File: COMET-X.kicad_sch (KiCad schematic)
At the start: 17 parts, among them J1 ATX_12V_IN, U2 TPS5450ddar

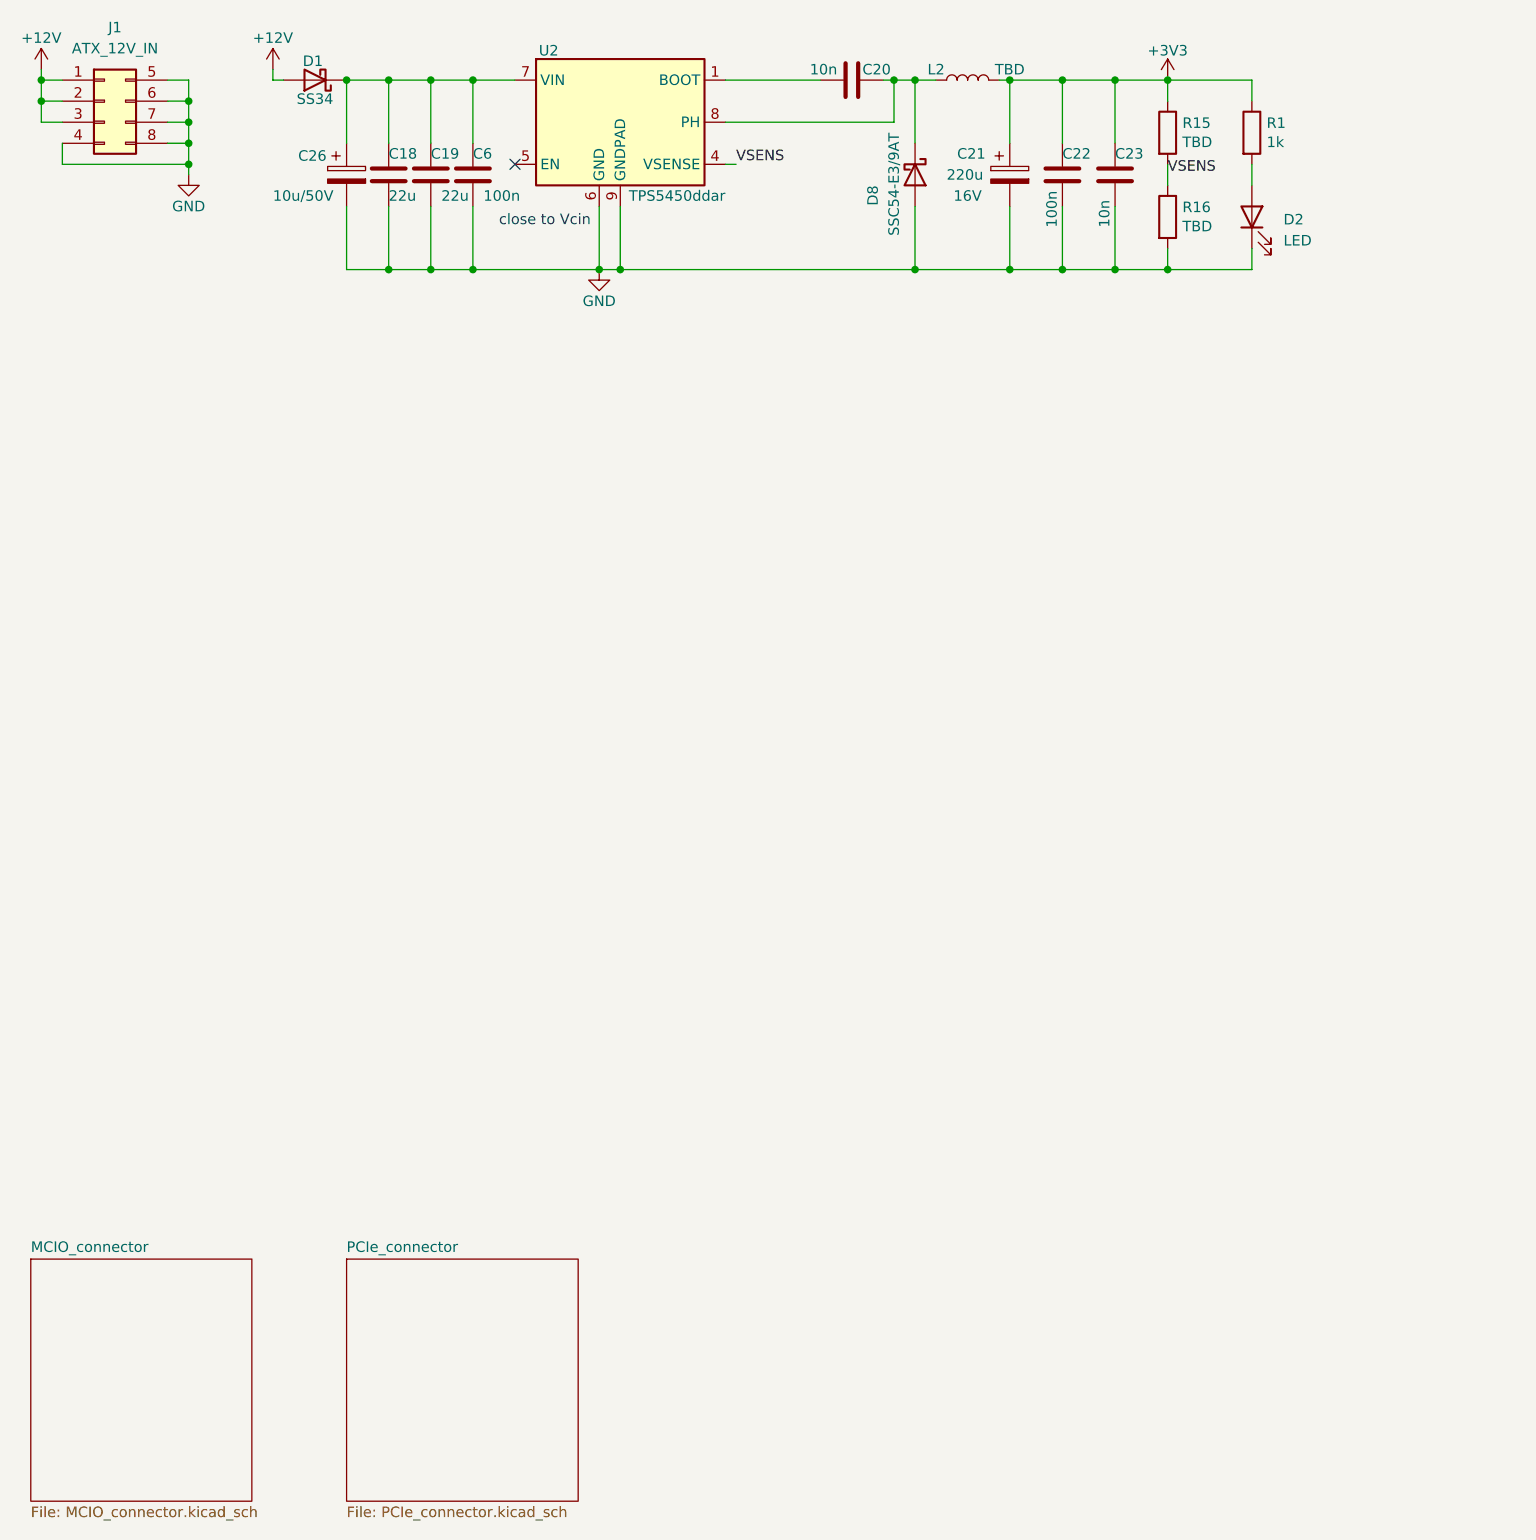
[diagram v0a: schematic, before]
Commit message: updated stackup and regulator
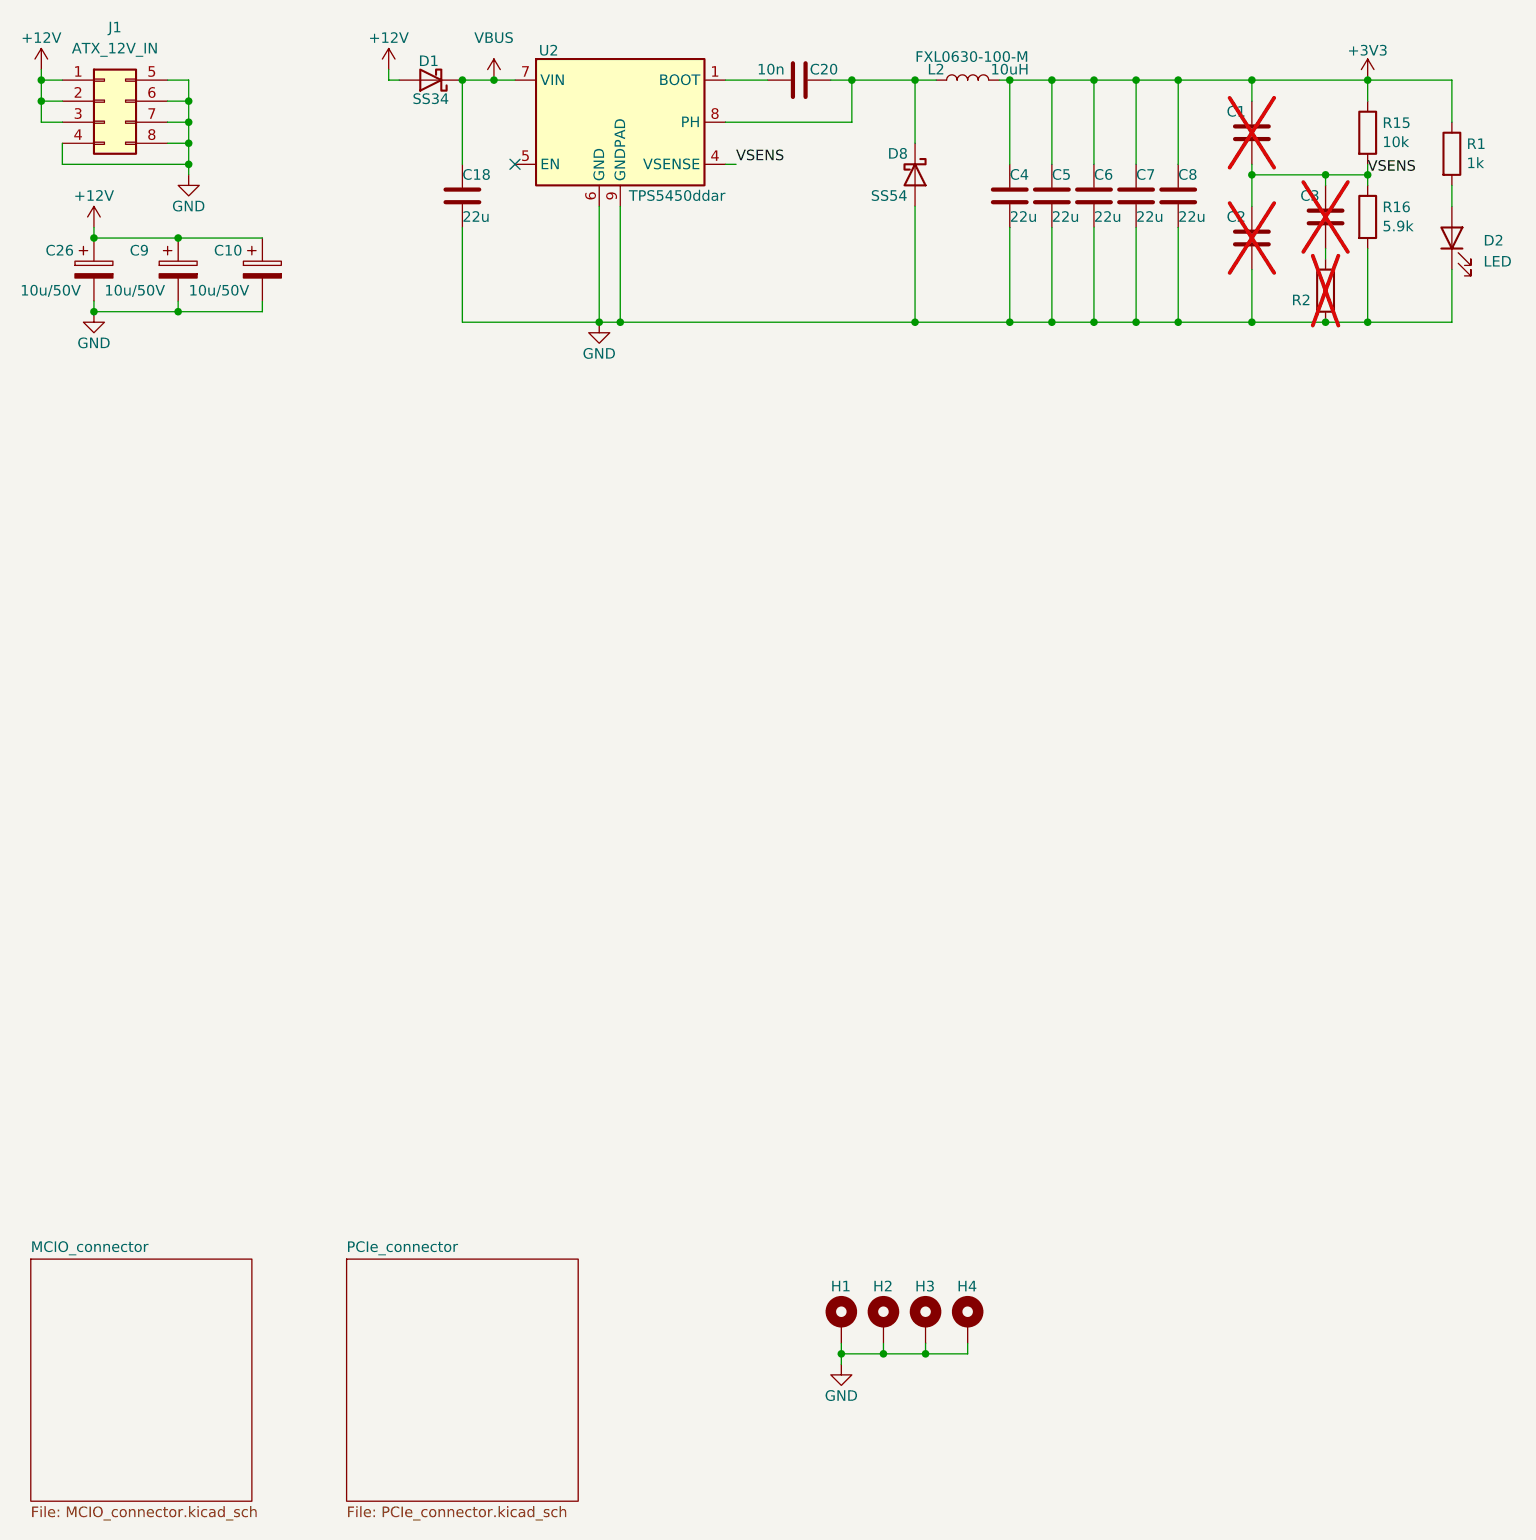
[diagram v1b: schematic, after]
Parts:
- removed C19: 22u, Capacitor_SMD:C_1206_3216Metric, symbol Device:C
- removed C21: 220u, Capacitor_SMD:CP_Elec_8x11.9, symbol Device:C_Polarized
- removed C22: 100n, Capacitor_SMD:C_0805_2012Metric, symbol Device:C
- removed C23: 10n, Capacitor_SMD:C_0805_2012Metric, symbol Device:C
- added C1, C2, C3: ~, Capacitor_SMD:C_0603_1608Metric, symbol Device:C
- added C10, C9: 10u/50V, Capacitor_SMD:CP_Elec_5x5.4, symbol Device:C_Polarized
- added C4, C5, C7, C8: 22u, Capacitor_SMD:C_1206_3216Metric, symbol Device:C
- added H1, H2, H3, H4: ~, MountingHole:MountingHole_3.2mm_M3_Pad_Via, symbol Mechanical:MountingHole_Pad
- added R2: ~, Resistor_SMD:R_0603_1608Metric, symbol Device:R
- C20: footprint Capacitor_SMD:C_0805_2012Metric -> Capacitor_SMD:C_0603_1608Metric
- C6: value 100n -> 22u; footprint Capacitor_SMD:C_0805_2012Metric -> Capacitor_SMD:C_1206_3216Metric
- D8: value SSC54-E3/9AT -> SS54; footprint Diode_SMD:D_SMC -> Diode_SMD:D_SMA
- L2: value TBD -> 10uH; footprint Inductor_SMD:L_Wuerth_HCI-1030 -> Inductor_SMD:L_Changjiang_FXL0630
- R15: value TBD -> 10k
- R16: value TBD -> 5.9k
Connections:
- net +12V: now also C26.1, C10.1, C9.1
- net +3V3: now also C6.1, C1.1, C4.1, C5.1, C7.1, C8.1
- net GND: now also C10.2, C2.2, C4.2, C5.2, C7.2, C8.2, C9.2, H1.1, H2.1, H3.1, H4.1, R2.1
- net VSENS: now also C1.2, C2.1, C3.1
- net VBUS: now reaches C18.1, D1.1 (K), U2.7 (VIN)
- net VBUS: no longer C26.1, C6.1
- new net: C3.2, R2.2
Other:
- note removed: "close to Vcin"
- moved on the sheet: C18, C20, C26, D1, D2, R1, R15, R16
